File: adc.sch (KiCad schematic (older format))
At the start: 7 parts, among them U301 ADS1261BIRHBR

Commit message: set up for reviewers
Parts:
- C202, C204, C205: LCSC (none) -> C28323
- C301: LCSC (none) -> C50131
- C303, C306: LCSC (none) -> C46653
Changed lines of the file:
@@
 F 2 "Capacitor_SMD:C_0805_2012Metric_Pad1.15x1.40mm_HandSolder" H 6138 1800 50  0001 C CNN
 F 3 "~" H 6100 1950 50  0001 C CNN
+F 4 "C28323" H 6100 1950 50  0001 C CNN "LCSC"
 	1    6100 1950
 	1    0    0    -1
@@
 F 2 "Capacitor_SMD:C_0805_2012Metric_Pad1.15x1.40mm_HandSolder" H 3638 5400 50  0001 C CNN
 F 3 "~" H 3600 5550 50  0001 C CNN
+F 4 "C50131" H 3600 5550 50  0001 C CNN "LCSC"
 	1    3600 5550
 	1    0    0    -1
@@
 F 2 "Capacitor_SMD:C_0805_2012Metric_Pad1.15x1.40mm_HandSolder" H 3388 5900 50  0001 C CNN
 F 3 "~" H 3350 6050 50  0001 C CNN
+F 4 "C28323" H 3350 6050 50  0001 C CNN "LCSC"
 	1    3350 6050
 	1    0    0    -1
@@
 F 2 "Capacitor_SMD:C_0805_2012Metric_Pad1.15x1.40mm_HandSolder" H 6088 5650 50  0001 C CNN
 F 3 "~" H 6050 5800 50  0001 C CNN
+F 4 "C28323" H 6050 5800 50  0001 C CNN "LCSC"
 	1    6050 5800
 	1    0    0    -1
@@
 F 2 "Capacitor_SMD:C_0805_2012Metric_Pad1.15x1.40mm_HandSolder" H 3738 5900 50  0001 C CNN
 F 3 "~" H 3700 6050 50  0001 C CNN
+F 4 "C46653" H 3700 6050 50  0001 C CNN "LCSC"
 	1    3700 6050
 	1    0    0    -1
@@
 F 2 "Capacitor_SMD:C_0805_2012Metric_Pad1.15x1.40mm_HandSolder" H 5988 3600 50  0001 C CNN
 F 3 "~" H 5950 3750 50  0001 C CNN
+F 4 "C46653" H 5950 3750 50  0001 C CNN "LCSC"
 	1    5950 3750
 	1    0    0    -1

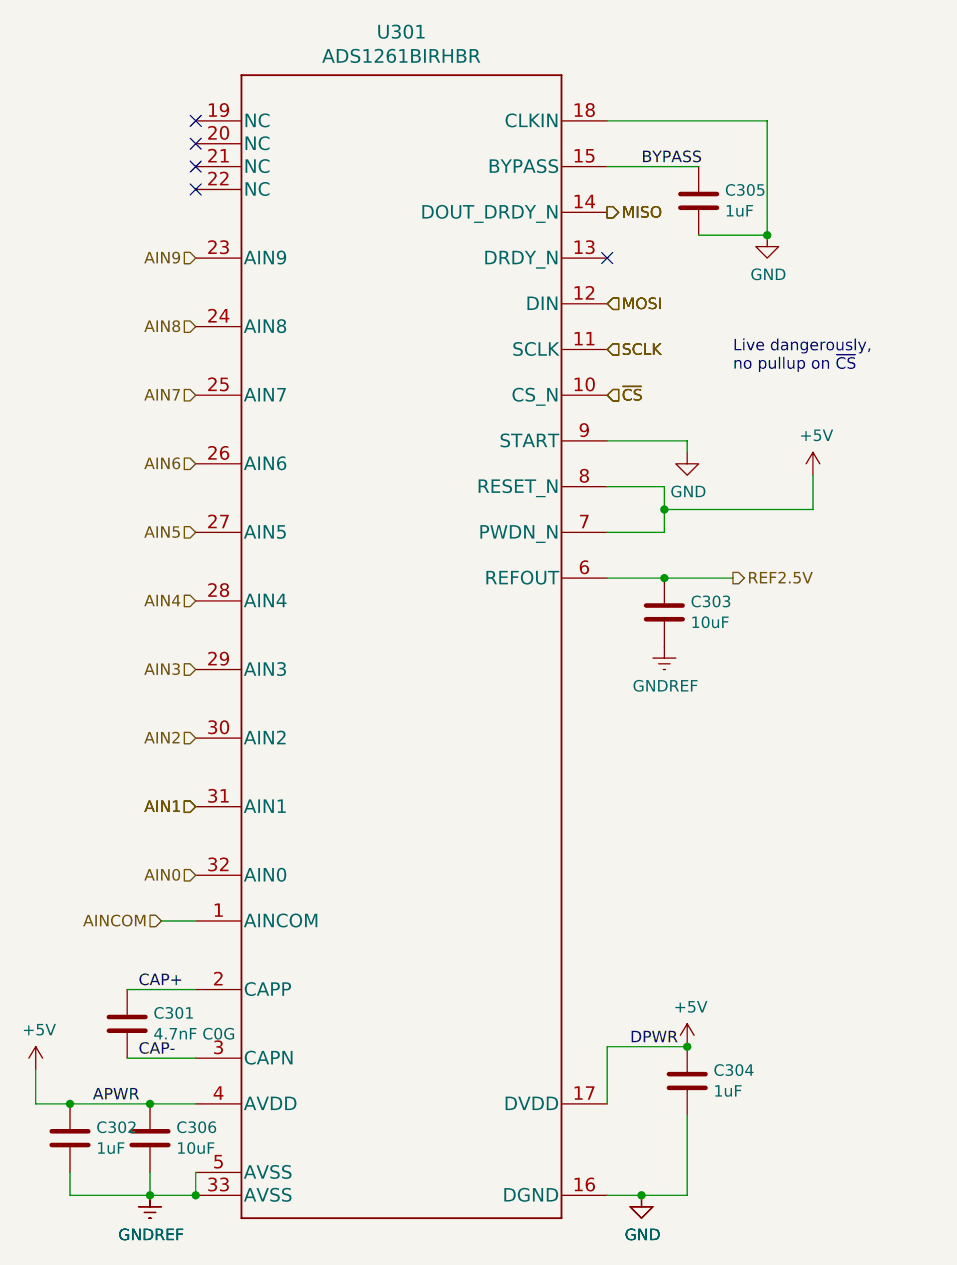
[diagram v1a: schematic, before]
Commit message: slid the header to the right, and set IO to 3.3V
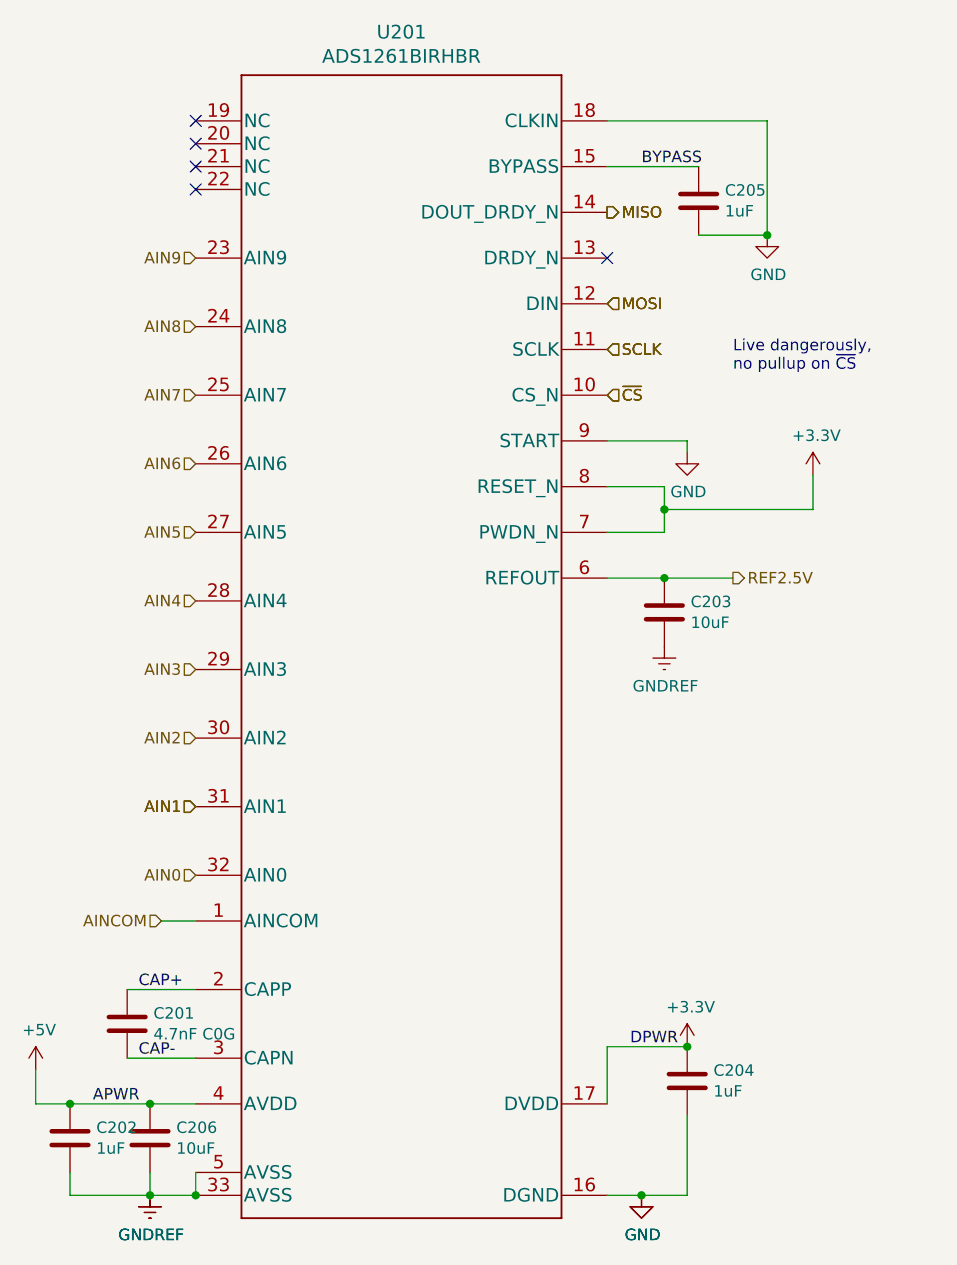
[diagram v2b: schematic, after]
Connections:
- net +5V: no longer C204.1, U301.17 (DVDD), U301.7 (PWDN_N), U301.8 (RESET_N)
- new net +3V3: C204.1, U301.17 (DVDD), U301.7 (PWDN_N), U301.8 (RESET_N)
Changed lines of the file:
@@
 $Descr A4 11693 8268
 encoding utf-8
-Sheet 3 4
+Sheet 2 4
 Title ""
 Date ""
@@
 AR Path="/5F4A8EC5/5F4B6004" Ref="C205"  Part="1"
 AR Path="/5F4D3EB7/5F4B6004" Ref="C305"  Part="1"
-F 0 "C305" H 6215 1996 50  0000 L CNN
+F 0 "C205" H 6215 1996 50  0000 L CNN
 F 1 "1uF" H 6215 1905 50  0000 L CNN
 F 2 "Capacitor_SMD:C_0805_2012Metric_Pad1.15x1.40mm_HandSolder" H 6138 1800 50  0001 C CNN
@@
 AR Path="/5F4D3EB7/5F4A90E1" Ref="U301"  Part="1"
 AR Path="/5F4A8EC5/5F4A90E1" Ref="U201"  Part="1"
-F 0 "U301" H 4800 6588 60  0000 C CNN
+F 0 "U201" H 4800 6588 60  0000 C CNN
 F 1 "ADS1261BIRHBR" H 4800 6482 60  0000 C CNN
 F 2 "Package_DFN_QFN:Texas_S-PVQFN-N32_EP3.45x3.45mm" H 4800 3840 60  0001 C CNN
@@
 AR Path="/5F4D3EB7/5F4AAB9D" Ref="C301"  Part="1"
 AR Path="/5F4A8EC5/5F4AAB9D" Ref="C201"  Part="1"
-F 0 "C301" H 3715 5596 50  0000 L CNN
+F 0 "C201" H 3715 5596 50  0000 L CNN
 F 1 "4.7nF C0G" H 3715 5505 50  0000 L CNN
 F 2 "Capacitor_SMD:C_0805_2012Metric_Pad1.15x1.40mm_HandSolder" H 3638 5400 50  0001 C CNN
@@
 AR Path="/5F4A8EC5/5F4B7BDA" Ref="C202"  Part="1"
 AR Path="/5F4D3EB7/5F4B7BDA" Ref="C302"  Part="1"
-F 0 "C302" H 3465 6096 50  0000 L CNN
+F 0 "C202" H 3465 6096 50  0000 L CNN
 F 1 "1uF" H 3465 6005 50  0000 L CNN
 F 2 "Capacitor_SMD:C_0805_2012Metric_Pad1.15x1.40mm_HandSolder" H 3388 5900 50  0001 C CNN
@@
 AR Path="/5F4A8EC5/5F4CD7CF" Ref="C204"  Part="1"
 AR Path="/5F4D3EB7/5F4CD7CF" Ref="C304"  Part="1"
-F 0 "C304" H 6165 5846 50  0000 L CNN
+F 0 "C204" H 6165 5846 50  0000 L CNN
 F 1 "1uF" H 6165 5755 50  0000 L CNN
 F 2 "Capacitor_SMD:C_0805_2012Metric_Pad1.15x1.40mm_HandSolder" H 6088 5650 50  0001 C CNN
@@
 AR Path="/5F4D3EB7/5F4C2005" Ref="C306"  Part="1"
 AR Path="/5F4A8EC5/5F4C2005" Ref="C206"  Part="1"
-F 0 "C306" H 3815 6096 50  0000 L CNN
+F 0 "C206" H 3815 6096 50  0000 L CNN
 F 1 "10uF" H 3815 6005 50  0000 L CNN
 F 2 "Capacitor_SMD:C_0805_2012Metric_Pad1.15x1.40mm_HandSolder" H 3738 5900 50  0001 C CNN
@@
 AR Path="/5F4D3EB7/5F4B8109" Ref="C303"  Part="1"
 AR Path="/5F4A8EC5/5F4B8109" Ref="C203"  Part="1"
-F 0 "C303" H 6065 3796 50  0000 L CNN
+F 0 "C203" H 6065 3796 50  0000 L CNN
 F 1 "10uF" H 6065 3705 50  0000 L CNN
 F 2 "Capacitor_SMD:C_0805_2012Metric_Pad1.15x1.40mm_HandSolder" H 5988 3600 50  0001 C CNN
@@
 Live dangerously,\nno pullup on ~CS
 $Comp
-L power:+5V #PWR0107
-U 1 1 5F81618F
+L power:+3.3V #PWR0104
+U 1 1 5FD0661D
+P 6050 5650
+AR Path="/5F4A8EC5/5FD0661D" Ref="#PWR0104"  Part="1"
+AR Path="/5F4D3EB7/5FD0661D" Ref="#PWR0107"  Part="1"
+F 0 "#PWR0107" H 6050 5500 50  0001 C CNN
+F 1 "+3.3V" H 6065 5823 50  0000 C CNN
+F 2 "" H 6050 5650 50  0001 C CNN
+F 3 "" H 6050 5650 50  0001 C CNN
+	1    6050 5650
+	1    0    0    -1
+$EndComp
+Connection ~ 6050 5650
+$Comp
+L power:+3.3V #PWR0105
+U 1 1 5FD07BF8
 P 6600 3150
-AR Path="/5F4D3EB7/5F81618F" Ref="#PWR0107"  Part="1"
-AR Path="/5F4A8EC5/5F81618F" Ref="#PWR0104"  Part="1"
-F 0 "#PWR0107" H 6600 3000 50  0001 C CNN
-F 1 "+5V" H 6615 3323 50  0000 C CNN
+AR Path="/5F4A8EC5/5FD07BF8" Ref="#PWR0105"  Part="1"
+AR Path="/5F4D3EB7/5FD07BF8" Ref="#PWR0110"  Part="1"
+F 0 "#PWR0110" H 6600 3000 50  0001 C CNN
+F 1 "+3.3V" H 6615 3323 50  0000 C CNN
 F 2 "" H 6600 3150 50  0001 C CNN
 F 3 "" H 6600 3150 50  0001 C CNN
@@
 	1    0    0    -1
 $EndComp
-$Comp
-L power:+5V #PWR0110
-U 1 1 5F817385
-P 6050 5650
-AR Path="/5F4D3EB7/5F817385" Ref="#PWR0110"  Part="1"
-AR Path="/5F4A8EC5/5F817385" Ref="#PWR0105"  Part="1"
-F 0 "#PWR0110" H 6050 5500 50  0001 C CNN
-F 1 "+5V" H 6065 5823 50  0000 C CNN
-F 2 "" H 6050 5650 50  0001 C CNN
-F 3 "" H 6050 5650 50  0001 C CNN
-	1    6050 5650
-	1    0    0    -1
-$EndComp
-Connection ~ 6050 5650
 $EndSCHEMATC
